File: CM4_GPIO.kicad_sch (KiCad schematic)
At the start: 28 parts, among them J11 RTC Battery Port, J12 RTC Battery Conn, J14 4x nano-fit, J3 2222, SW1 SW_Push, SW2 SW_Push

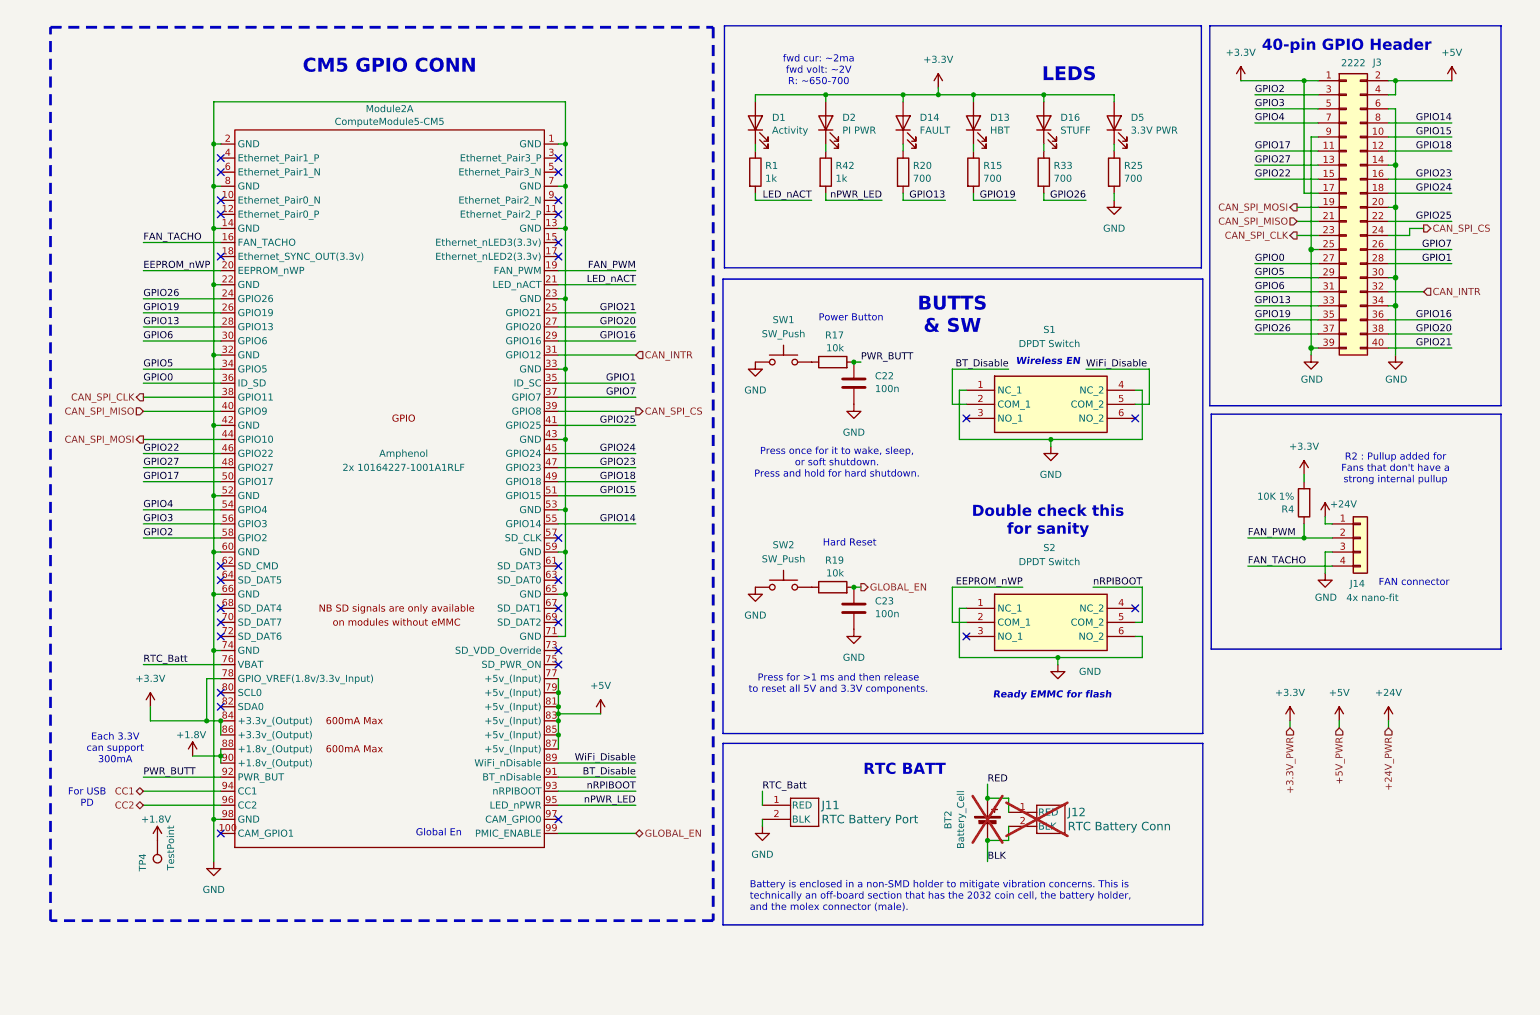
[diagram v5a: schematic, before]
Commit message: moved things to their own sheets
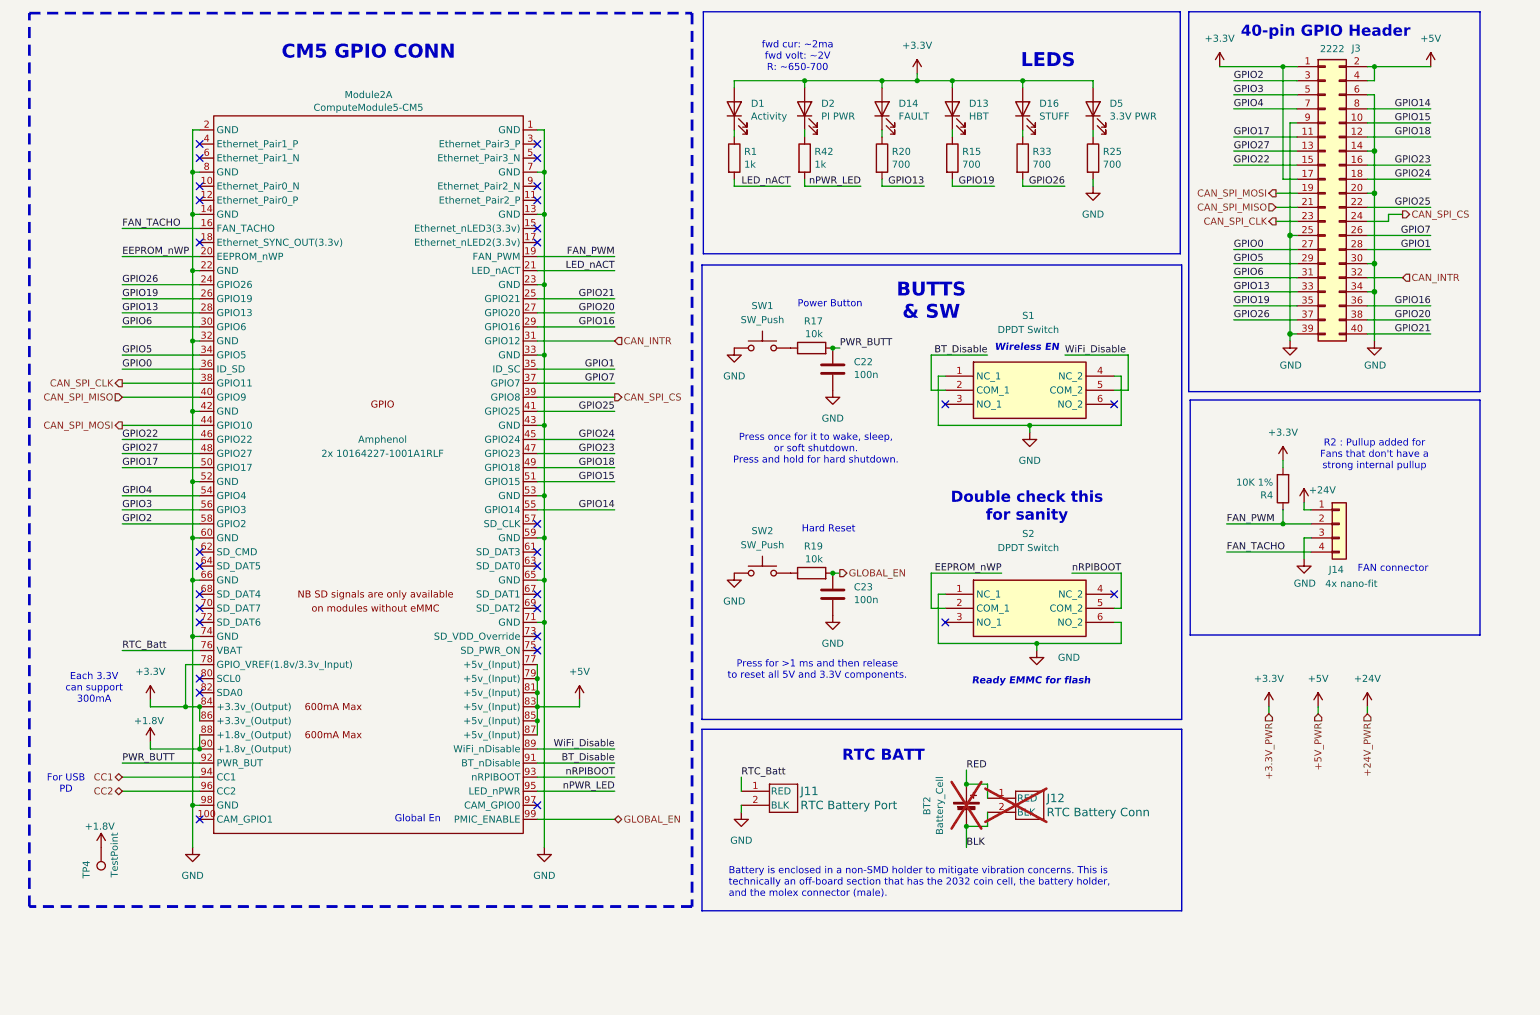
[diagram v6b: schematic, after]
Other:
- moved on the sheet: BT2, C22, C23, D1, D13, D14, D16, D2, D5, J11, J12, J14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
